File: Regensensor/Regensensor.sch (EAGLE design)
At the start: 35 parts, among them IC1 LM358N, K1 SMI-2P, T1 BC337, T2 BC327, X1 Output, X2 Heating, X3 Sensor, X4 Supply

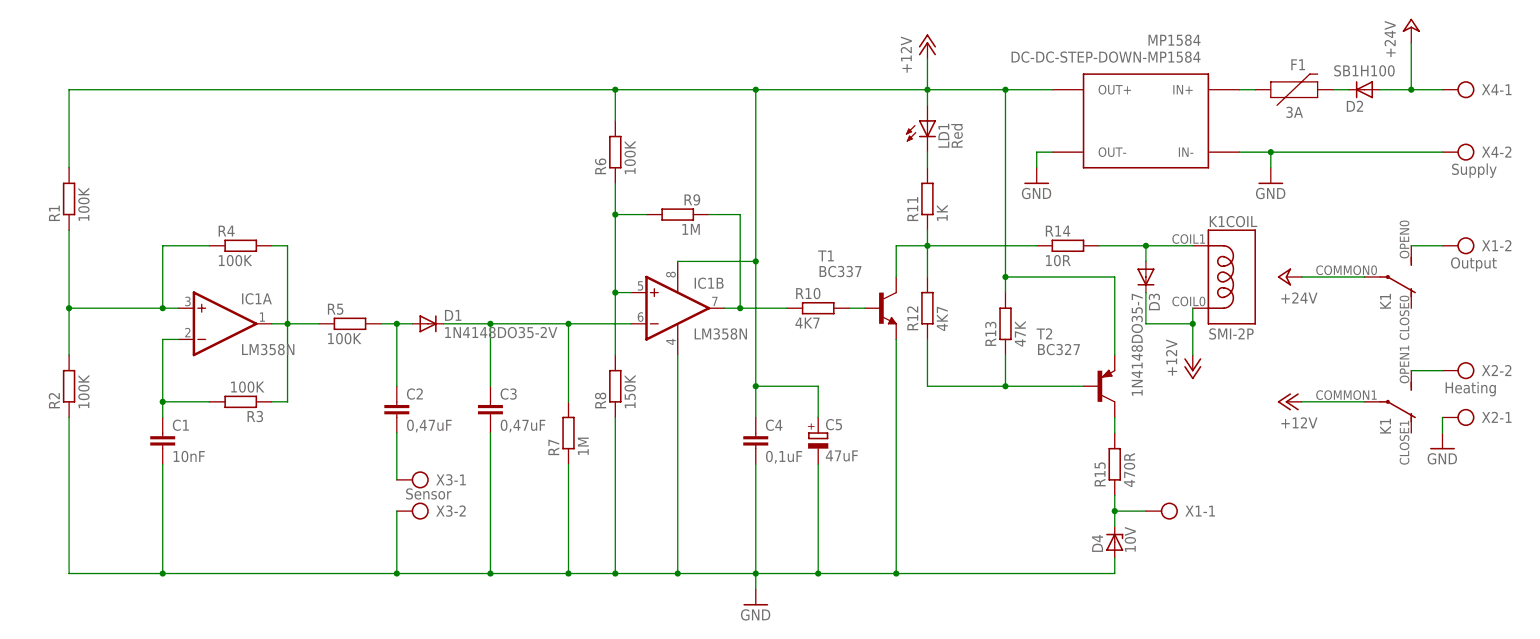
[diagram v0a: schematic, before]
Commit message: Rework rain sensor board and make it ready for production.
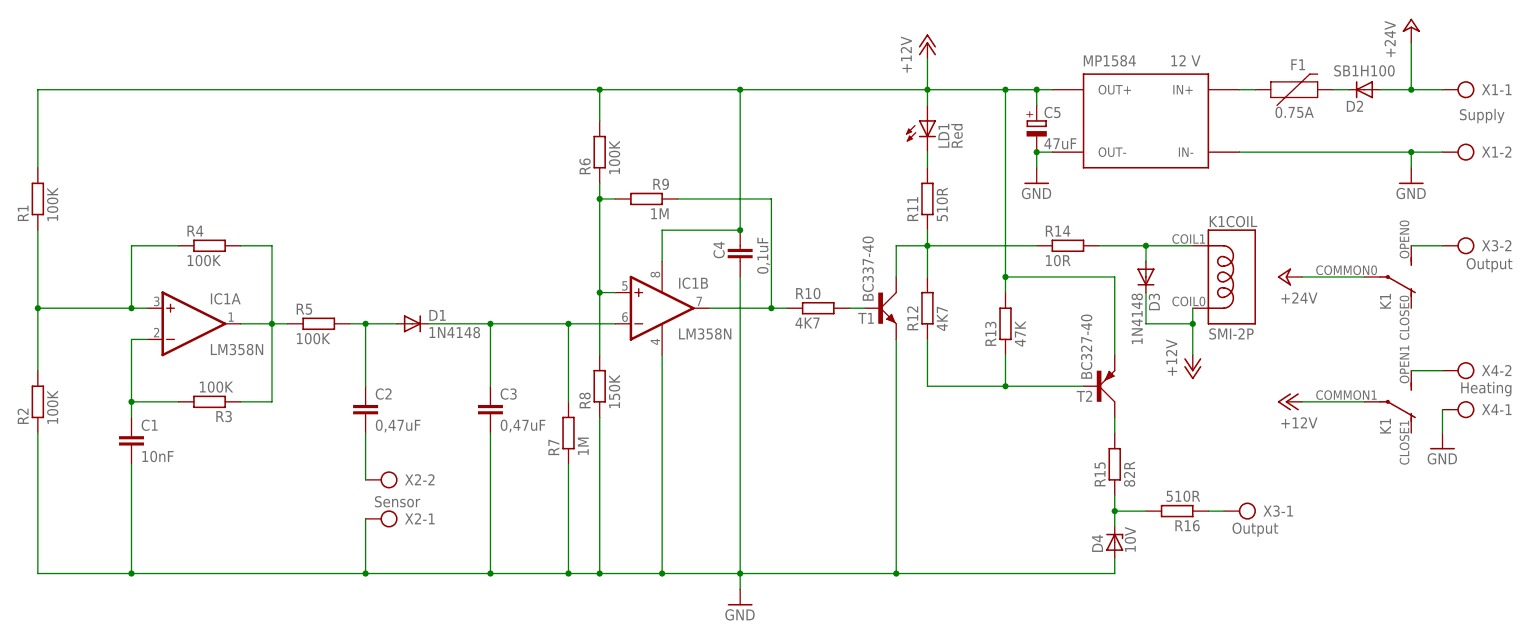
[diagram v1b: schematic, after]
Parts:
- added R16: 510R, rcl:R-EU_0204/2V
- C1: device rcl:C-EU050-025X075 -> rcl:C-EU050-055X075
- C2, C3: device rcl:C-EU050-025X075 -> rcl:C-EU050-035X075
- C4: device rcl:C-EU050-025X075 -> rcl:C-EU025-030X050
- C5: device rcl:CPOL-EUE5-6 -> rcl:CPOL-EUE2.5-7
- D1: value 1N4148DO35-2V -> 1N4148
- D3: value 1N4148DO35-7 -> 1N4148
- F1: value 3A -> 0.75A; device SparkFun-Fuses:PPTCPTH11MM -> ptc:PPTCRGEF250
- MP1584: value DC-DC-STEP-DOWN-MP1584 -> 12 V; device modules:DC-DC-STEP-DOWN-MP1584 -> modules:DC-DC-STEP-DOWNMP1584
- R1, R2, R3: device rcl:R-EU_0207/2V -> rcl:R-EU_0204/2V
- R10, R4, R6, R9: device rcl:R-EU_0207/2V -> rcl:R-EU_0204/5
- R11: value 1K -> 510R; device rcl:R-EU_0207/2V -> rcl:R-EU_0204/2V
- R12, R14: device rcl:R-EU_0207/5V -> rcl:R-EU_0204/2V
- R15: value 470R -> 82R; device rcl:R-EU_0207/7 -> rcl:R-EU_0204/2V
- R5: device rcl:R-EU_0207/7 -> rcl:R-EU_0204/2V
- R7: device rcl:R-EU_0204/5 -> rcl:R-EU_0204/2V
- R8: device rcl:R-EU_0207/5V -> rcl:R-EU_0204/5
- T1: value BC337 -> BC337-40; device transistor-npn:BC337 -> transistor-small-signal:BC337LINE
- T2: value BC327 -> BC327-40; device transistor-pnp:BC327 -> transistor-small-signal:BC327LINE
- X1: value Output -> Supply; device con-ptr500:AK500/2 -> con-phoenix-mkds-3:MKDS-3/25,08
- X2: value Heating -> Sensor; device con-ptr500:AK500/2 -> con-phoenix-mkds-3:MKDS-3/25,08
- X3: value Sensor -> Output; device con-ptr500:AK500/2 -> con-phoenix-mkds-3:MKDS-3/25,08
- X4: value Supply -> Heating; device con-ptr500:AK500/2 -> con-phoenix-mkds-3:MKDS-3/25,08
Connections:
- new net N$20: R16.1, X3-1.KL
- net +24V: now also X1-1.KL; no longer X4-1.KL
- net GND: now also X1-2.KL, X4-1.KL; no longer X3-2.KL, X4-2.KL
- net N$13: now also X2-2.KL; no longer X3-1.KL
- net N$15: now also R16.2; no longer X1-1.KL
- net N$16: now also X3-2.KL; no longer X1-2.KL
- net N$17: now also X4-2.KL; no longer X2-2.KL
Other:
- note added: "Output"
- moved on the sheet: C1, C2, C4, C5, D1, IC1A, IC1B, R1, R2, R3, R4, R5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

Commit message: Fix rain sensor capacitor footprint
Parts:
- C5: device rcl:CPOL-EUE2.5-7 -> rcl:CPOL-EUE5-6
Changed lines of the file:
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@@
 <grid distance="0.1" unitdist="inch" unit="inch" style="lines" multiple="1" display="no" altdistance="0.01" altunitdist="inch" altunit="inch"/>
 <layers>
-<layer number="1" name="Top" color="4" fill="1" visible="no" active="no"/>
-<layer number="16" name="Bottom" color="1" fill="1" visible="no" active="no"/>
-<layer number="17" name="Pads" color="2" fill="1" visible="no" active="no"/>
-<layer number="18" name="Vias" color="2" fill="1" visible="no" active="no"/>
-<layer number="19" name="Unrouted" color="6" fill="1" visible="no" active="no"/>
-<layer number="20" name="Dimension" color="15" fill="1" visible="no" active="no"/>
-<layer number="21" name="tPlace" color="7" fill="1" visible="no" active="no"/>
-<layer number="22" name="bPlace" color="7" fill="1" visible="no" active="no"/>
-<layer number="23" name="tOrigins" color="15" fill="1" visible="no" active="no"/>
-<layer number="24" name="bOrigins" color="15" fill="1" visible="no" active="no"/>
-<layer number="25" name="tNames" color="7" fill="1" visible="no" active="no"/>
-<layer number="26" name="bNames" color="7" fill="1" visible="no" active="no"/>
-<layer number="27" name="tValues" color="7" fill="1" visible="no" active="no"/>
-<layer number="28" name="bValues" color="7" fill="1" visible="no" active="no"/>
+<layer number="1" name="Top" color="4" fill="1" visible="yes" active="no"/>
+<layer number="16" name="Bottom" color="1" fill="1" visible="yes" active="no"/>
+<layer number="17" name="Pads" color="2" fill="1" visible="yes" active="no"/>
+<layer number="18" name="Vias" color="2" fill="1" visible="yes" active="no"/>
+<layer number="19" name="Unrouted" color="6" fill="1" visible="yes" active="no"/>
+<layer number="20" name="Dimension" color="15" fill="1" visible="yes" active="no"/>
+<layer number="21" name="tPlace" color="7" fill="1" visible="yes" active="no"/>
+<layer number="22" name="bPlace" color="7" fill="1" visible="yes" active="no"/>
+<layer number="23" name="tOrigins" color="15" fill="1" visible="yes" active="no"/>
+<layer number="24" name="bOrigins" color="15" fill="1" visible="yes" active="no"/>
+<layer number="25" name="tNames" color="7" fill="1" visible="yes" active="no"/>
+<layer number="26" name="bNames" color="7" fill="1" visible="yes" active="no"/>
+<layer number="27" name="tValues" color="7" fill="1" visible="yes" active="no"/>
+<layer number="28" name="bValues" color="7" fill="1" visible="yes" active="no"/>
 <layer number="29" name="tStop" color="7" fill="3" visible="no" active="no"/>
 <layer number="30" name="bStop" color="7" fill="6" visible="no" active="no"/>
@@
 <layer number="35" name="tGlue" color="7" fill="4" visible="no" active="no"/>
 <layer number="36" name="bGlue" color="7" fill="5" visible="no" active="no"/>
-<layer number="37" name="tTest" color="7" fill="1" visible="no" active="no"/>
-<layer number="38" name="bTest" color="7" fill="1" visible="no" active="no"/>
+<layer number="37" name="tTest" color="7" fill="1" visible="yes" active="no"/>
+<layer number="38" name="bTest" color="7" fill="1" visible="yes" active="no"/>
 <layer number="39" name="tKeepout" color="4" fill="11" visible="no" active="no"/>
 <layer number="40" name="bKeepout" color="1" fill="11" visible="no" active="no"/>
@@
 <layer number="44" name="Drills" color="7" fill="1" visible="no" active="no"/>
 <layer number="45" name="Holes" color="7" fill="1" visible="no" active="no"/>
-<layer number="46" name="Milling" color="3" fill="1" visible="no" active="no"/>
-<layer number="47" name="Measures" color="7" fill="1" visible="no" active="no"/>
-<layer number="48" name="Document" color="7" fill="1" visible="no" active="no"/>
-<layer number="49" name="Reference" color="7" fill="1" visible="no" active="no"/>
-<layer number="50" name="dxf" color="7" fill="1" visible="no" active="no"/>
-<layer number="51" name="tDocu" color="7" fill="1" visible="no" active="no"/>
-<layer number="52" name="bDocu" color="7" fill="1" visible="no" active="no"/>
-<layer number="53" name="tGND_GNDA" color="7" fill="9" visible="no" active="no"/>
-<layer number="54" name="bGND_GNDA" color="1" fill="9" visible="no" active="no"/>
-<layer number="56" name="wert" color="7" fill="1" visible="no" active="no"/>
-<layer number="57" name="tCAD" color="7" fill="1" visible="no" active="no"/>
-<layer number="59" name="tCarbon" color="7" fill="1" visible="no" active="no"/>
-<layer number="60" name="bCarbon" color="7" fill="1" visible="no" active="no"/>
+<layer number="46" name="Milling" color="3" fill="1" visible="yes" active="no"/>
+<layer number="47" name="Measures" color="7" fill="1" visible="yes" active="no"/>
+<layer number="48" name="Document" color="7" fill="1" visible="yes" active="no"/>
+<layer number="49" name="Reference" color="7" fill="1" visible="yes" active="no"/>
+<layer number="50" name="dxf" color="7" fill="1" visible="yes" active="no"/>
+<layer number="51" name="tDocu" color="7" fill="1" visible="yes" active="no"/>
+<layer number="52" name="bDocu" color="7" fill="1" visible="yes" active="no"/>
+<layer number="53" name="tGND_GNDA" color="7" fill="9" visible="yes" active="no"/>
+<layer number="54" name="bGND_GNDA" color="1" fill="9" visible="yes" active="no"/>
+<layer number="56" name="wert" color="7" fill="1" visible="yes" active="no"/>
+<layer number="57" name="tCAD" color="7" fill="1" visible="yes" active="no"/>
+<layer number="59" name="tCarbon" color="7" fill="1" visible="yes" active="no"/>
+<layer number="60" name="bCarbon" color="7" fill="1" visible="yes" active="no"/>
 <layer number="90" name="Modules" color="5" fill="1" visible="yes" active="yes"/>
 <layer number="91" name="Nets" color="2" fill="1" visible="yes" active="yes"/>
@@
 <part name="R14" library="rcl" deviceset="R-EU_" device="0204/2V" value="10R"/>
 <part name="R13" library="rcl" deviceset="R-EU_" device="0204/2V" value="47K"/>
-<part name="C5" library="rcl" deviceset="CPOL-EU" device="E2.5-7" value="47uF"/>
+<part name="C5" library="rcl" deviceset="CPOL-EU" device="E5-6" value="47uF"/>
 <part name="X2" library="con-phoenix-mkds-3" deviceset="MKDS-3/2" device="5,08" value="Sensor"/>
 <part name="X4" library="con-phoenix-mkds-3" deviceset="MKDS-3/2" device="5,08" value="Heating"/>
